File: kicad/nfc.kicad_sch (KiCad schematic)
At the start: 31 parts, among them IC3 PN7160A1HN_C100E, J5 Conn_01x06, J6 Conn_01x06, Y1 27.12MHz Crystal

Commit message: First revision
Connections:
- net NFC_GND: now also IC3.20 (VSS(TX))
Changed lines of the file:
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@@
+	)
+	(label "NFC_GND"
+		(at 107.95 124.46 270)
+		(effects
+			(font
+				(size 1.27 1.27)
+			)
+			(justify right bottom)
+		)
 	)
 	(label "NFC_GND"

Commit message: Added level shifter
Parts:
- renumbered R16 to R11
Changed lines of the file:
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@@
 		(dnp no)
 		(fields_autoplaced yes)
-		(property "Reference" "R16"
+		(property "Reference" "R11"
 			(at 232.41 63.5 90)
 			(effects
@@
 			(project "beacons"
 				(path "/5f965b21-e640-476e-a1f5-99fd6aaca14e/d94a807e-452b-4b4d-a56b-0922c476e41f"
-					(reference "R16")
+					(reference "R11")
 					(unit 1)
 				)

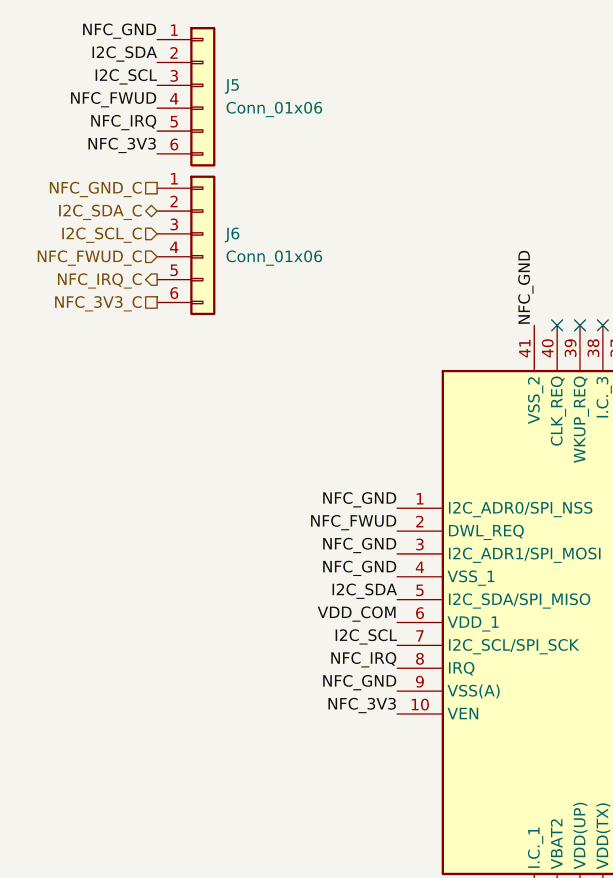
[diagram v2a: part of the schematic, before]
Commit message: Added NFC enable pin
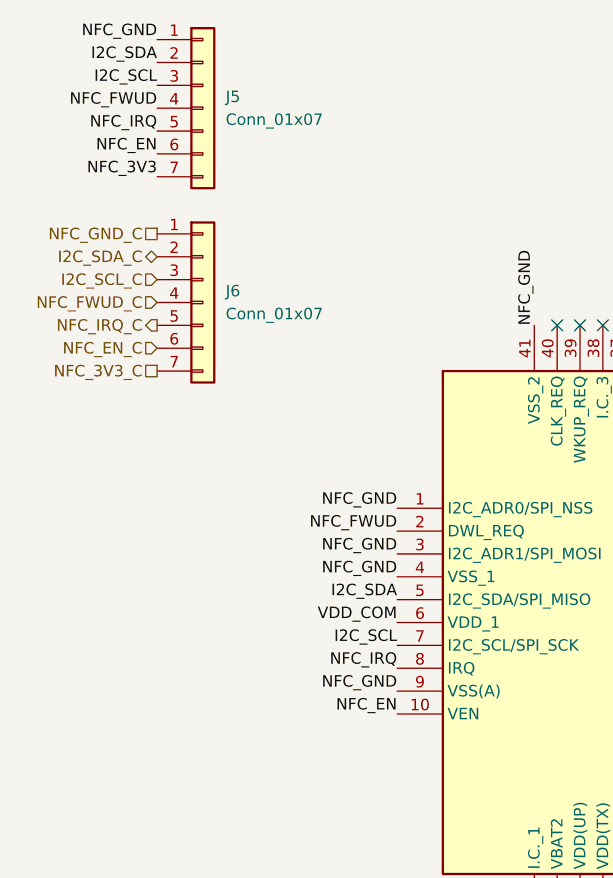
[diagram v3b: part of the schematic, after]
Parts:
- removed J5, J6: Conn_01x06, Connector_JST:JST_PH_B6B-PH-K_1x06_P2.00mm_Vertical, symbol Connector_Generic:Conn_01x06
- added J5, J6: Conn_01x07, Connector_JST:JST_PH_B7B-PH-K_1x07_P2.00mm_Vertical, symbol Connector_Generic:Conn_01x07
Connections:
- net I2C_SCL: now also J5.3 (Pin_3)
- net I2C_SCL_C: now also J6.3 (Pin_3)
- net I2C_SDA: now also J5.2 (Pin_2)
- net I2C_SDA_C: now also J6.2 (Pin_2)
- net NFC_3V3: now also J5.7 (Pin_7); no longer IC3.10 (VEN)
- net NFC_3V3_C: now also J6.7 (Pin_7)
- net NFC_FWUD: now also J5.4 (Pin_4)
- net NFC_FWUD_C: now also J6.4 (Pin_4)
- net NFC_GND: now also J5.1 (Pin_1)
- net NFC_GND_C: now also J6.1 (Pin_1)
- net NFC_IRQ: now also J5.5 (Pin_5)
- net NFC_IRQ_C: now also J6.5 (Pin_5)
- new net NFC_EN: IC3.10 (VEN), J5.6 (Pin_6)
- new net NFC_EN_C: J6.6 (Pin_6)
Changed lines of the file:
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@@
+		)
+	)
+	(label "NFC_EN"
+		(at 43.18 39.37 180)
+		(effects
+			(font
+				(size 1.27 1.27)
+			)
+			(justify right bottom)
 		)
 	)
@@
 		)
 	)
-	(label "NFC_3V3"
+	(label "NFC_EN"
 		(at 69.85 101.6 180)
 		(effects
@@
 		)
 	)
+	(label "NFC_3V3"
+		(at 43.18 41.91 180)
+		(effects
+			(font
+				(size 1.27 1.27)
+			)
+			(justify right bottom)
+		)
+	)
 	(label "I2C_SCL"
 		(at 43.18 31.75 180)
@@
 		)
 	)
-	(label "NFC_3V3"
-		(at 43.18 39.37 180)
-		(effects
-			(font
-				(size 1.27 1.27)
-			)
-			(justify right bottom)
-		)
-	)
 	(label "VDD_COM"
 		(at 127 58.42 0)
@@
 	(hierarchical_label "NFC_FWUD_C"
 		(shape input)
-		(at 43.18 50.8 180)
+		(at 43.18 55.88 180)
+		(effects
+			(font
+				(size 1.27 1.27)
+			)
+			(justify right)
+		)
+	)
+	(hierarchical_label "NFC_3V3_C"
+		(shape passive)
+		(at 43.18 63.5 180)
 		(effects
 			(font
@@
 	(hierarchical_label "I2C_SCL_C"
 		(shape input)
-		(at 43.18 48.26 180)
+		(at 43.18 53.34 180)
 		(effects
 			(font
@@
 	(hierarchical_label "NFC_IRQ_C"
 		(shape output)
-		(at 43.18 53.34 180)
+		(at 43.18 58.42 180)
+		(effects
+			(font
+				(size 1.27 1.27)
+			)
+			(justify right)
+		)
+	)
+	(hierarchical_label "NFC_EN_C"
+		(shape input)
+		(at 43.18 60.96 180)
 		(effects
 			(font
@@
 	(hierarchical_label "I2C_SDA_C"
 		(shape bidirectional)
-		(at 43.18 45.72 180)
-		(effects
-			(font
-				(size 1.27 1.27)
-			)
-			(justify right)
-		)
-	)
-	(hierarchical_label "NFC_3V3_C"
-		(shape passive)
-		(at 43.18 55.88 180)
+		(at 43.18 50.8 180)
 		(effects
 			(font
@@
 	(hierarchical_label "NFC_GND_C"
 		(shape passive)
-		(at 43.18 43.18 180)
+		(at 43.18 48.26 180)
 		(effects
 			(font
@@
 	)
 	(symbol
+		(lib_id "Connector_Generic:Conn_01x07")
+		(at 48.26 34.29 0)
+		(unit 1)
+		(exclude_from_sim no)
+		(in_bom yes)
+		(on_board yes)
+		(dnp no)
+		(fields_autoplaced yes)
+		(property "Reference" "J5"
+			(at 50.8 33.0199 0)
+			(effects
+				(font
+					(size 1.27 1.27)
+				)
+				(justify left)
+			)
+		)
+		(property "Value" "Conn_01x07"
+			(at 50.8 35.5599 0)
+			(effects
+				(font
+					(size 1.27 1.27)
+				)
+				(justify left)
+			)
+		)
+		(property "Footprint" "Connector_JST:JST_PH_B7B-PH-K_1x07_P2.00mm_Vertical"
+			(at 48.26 34.29 0)
+			(effects
+				(font
+					(size 1.27 1.27)
+				)
+				(hide yes)
+			)
+		)
+		(property "Datasheet" "~"
+			(at 48.26 34.29 0)
+			(effects
+				(font
+					(size 1.27 1.27)
+				)
+				(hide yes)
+			)
+		)
+		(property "Description" "Generic connector, single row, 01x07, script generated (kicad-library-utils/schlib/autogen/connector/)"
+			(at 48.26 34.29 0)
+			(effects
+				(font
+					(size 1.27 1.27)
+				)
+				(hide yes)
+			)
+		)
+		(pin "5"
+		)
+		(pin "6"
+		)
+		(pin "7"
+		)
+		(pin "1"
+		)
+		(pin "2"
+		)
+		(pin "3"
+		)
+		(pin "4"
+		)
+		(instances
+			(project ""
+				(path "/5f965b21-e640-476e-a1f5-99fd6aaca14e/d94a807e-452b-4b4d-a56b-0922c476e41f"
+					(reference "J5")
+					(unit 1)
+				)
+			)
+		)
+	)
+	(symbol
 		(lib_id "Device:C")
 		(at 189.23 66.04 90)
@@
 	)
 	(symbol
-		(lib_id "Connector_Generic:Conn_01x06")
-		(at 48.26 48.26 0)
-		(unit 1)
-		(exclude_from_sim no)
-		(in_bom yes)
-		(on_board yes)
-		(dnp no)
-		(fields_autoplaced yes)
-		(property "Reference" "J6"
-			(at 50.8 48.2599 0)
-			(effects
-				(font
-					(size 1.27 1.27)
-				)
-				(justify left)
-			)
-		)
-		(property "Value" "Conn_01x06"
-			(at 50.8 50.7999 0)
-			(effects
-				(font
-					(size 1.27 1.27)
-				)
-				(justify left)
-			)
-		)
-		(property "Footprint" "Connector_JST:JST_PH_B6B-PH-K_1x06_P2.00mm_Vertical"
-			(at 48.26 48.26 0)
-			(effects
-				(font
-					(size 1.27 1.27)
-				)
-				(hide yes)
-			)
-		)
-		(property "Datasheet" "~"
-			(at 48.26 48.26 0)
-			(effects
-				(font
-					(size 1.27 1.27)
-				)
-				(hide yes)
-			)
-		)
-		(property "Description" "Generic connector, single row, 01x06, script generated (kicad-library-utils/schlib/autogen/connector/)"
-			(at 48.26 48.26 0)
-			(effects
-				(font
-					(size 1.27 1.27)
-				)
-				(hide yes)
-			)
-		)
-		(pin "6"
-		)
-		(pin "5"
-		)
-		(pin "3"
-		)
-		(pin "4"
-		)
-		(pin "2"
-		)
-		(pin "1"
-		)
-		(instances
-			(project "beacons"
-				(path "/5f965b21-e640-476e-a1f5-99fd6aaca14e/d94a807e-452b-4b4d-a56b-0922c476e41f"
-					(reference "J6")
-					(unit 1)
-				)
-			)
-		)
-	)
-	(symbol
 		(lib_id "Device:R")
 		(at 217.17 81.28 90)
@@
 	)
 	(symbol
+		(lib_id "Connector_Generic:Conn_01x07")
+		(at 48.26 55.88 0)
+		(unit 1)
+		(exclude_from_sim no)
+		(in_bom yes)
+		(on_board yes)
+		(dnp no)
+		(fields_autoplaced yes)
+		(property "Reference" "J6"
+			(at 50.8 54.6099 0)
+			(effects
+				(font
+					(size 1.27 1.27)
+				)
+				(justify left)
+			)
+		)
+		(property "Value" "Conn_01x07"
+			(at 50.8 57.1499 0)
+			(effects
+				(font
+					(size 1.27 1.27)
+				)
+				(justify left)
+			)
+		)
+		(property "Footprint" "Connector_JST:JST_PH_B7B-PH-K_1x07_P2.00mm_Vertical"
+			(at 48.26 55.88 0)
+			(effects
+				(font
+					(size 1.27 1.27)
+				)
+				(hide yes)
+			)
+		)
+		(property "Datasheet" "~"
+			(at 48.26 55.88 0)
+			(effects
+				(font
+					(size 1.27 1.27)
+				)
+				(hide yes)
+			)
+		)
+		(property "Description" "Generic connector, single row, 01x07, script generated (kicad-library-utils/schlib/autogen/connector/)"
+			(at 48.26 55.88 0)
+			(effects
+				(font
+					(size 1.27 1.27)
+				)
+				(hide yes)
+			)
+		)
+		(pin "5"
+		)
+		(pin "6"
+		)
+		(pin "7"
+		)
+		(pin "1"
+		)
+		(pin "2"
+		)
+		(pin "3"
+		)
+		(pin "4"
+		)
+		(instances
+			(project "beacons"
+				(path "/5f965b21-e640-476e-a1f5-99fd6aaca14e/d94a807e-452b-4b4d-a56b-0922c476e41f"
+					(reference "J6")
+					(unit 1)
+				)
+			)
+		)
+	)
+	(symbol
 		(lib_id "Device:C")
 		(at 204.47 77.47 0)
@@
 					(unit 1)
 				)
-			)
-		)
-	)
-	(symbol
-		(lib_id "Connector_Generic:Conn_01x06")
-		(at 48.26 31.75 0)
-		(unit 1)
-		(exclude_from_sim no)
-		(in_bom yes)
-		(on_board yes)
-		(dnp no)
-		(fields_autoplaced yes)
-		(property "Reference" "J5"
-			(at 50.8 31.7499 0)
-			(effects
-				(font
-					(size 1.27 1.27)
-				)
-				(justify left)
-			)
-		)
-		(property "Value" "Conn_01x06"
-			(at 50.8 34.2899 0)
-			(effects
-				(font
-					(size 1.27 1.27)
-				)
-				(justify left)
-			)
-		)
-		(property "Footprint" "Connector_JST:JST_PH_B6B-PH-K_1x06_P2.00mm_Vertical"
-			(at 48.26 31.75 0)
-			(effects
-				(font
-					(size 1.27 1.27)
-				)
-				(hide yes)
-			)
-		)
-		(property "Datasheet" "~"
-			(at 48.26 31.75 0)
-			(effects
-				(font
-					(size 1.27 1.27)
-				)
-				(hide yes)
-			)
-		)
-		(property "Description" "Generic connector, single row, 01x06, script generated (kicad-library-utils/schlib/autogen/connector/)"
-			(at 48.26 31.75 0)
-			(effects
-				(font
-					(size 1.27 1.27)
-				)
-				(hide yes)
-			)
-		)
-		(pin "6"
-		)
-		(pin "5"
-		)
-		(pin "3"
-		)
-		(pin "4"
-		)
-		(pin "2"
-		)
-		(pin "1"
-		)
-		(instances
-			(project ""
-				(path "/5f965b21-e640-476e-a1f5-99fd6aaca14e/d94a807e-452b-4b4d-a56b-0922c476e41f"
-					(reference "J5")
-					(unit 1)
-				)
